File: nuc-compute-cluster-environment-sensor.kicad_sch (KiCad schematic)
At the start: 104 parts

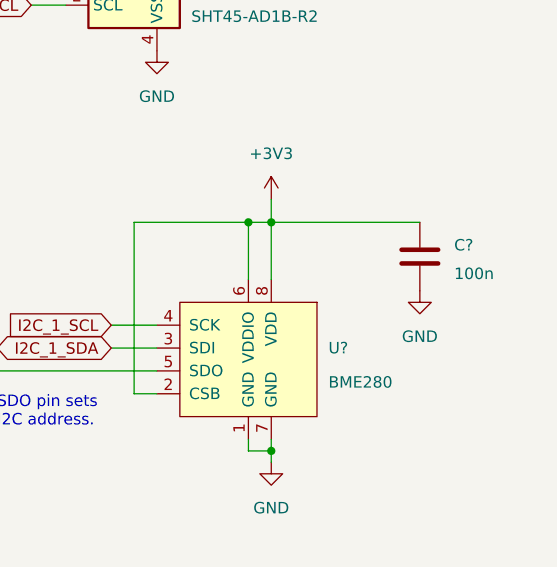
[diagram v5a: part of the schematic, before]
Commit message: [#39832] SCH: Add extra 100n cap to BME280 supply
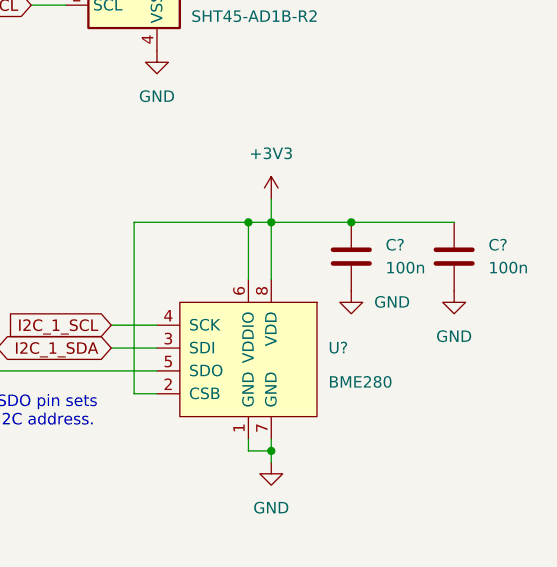
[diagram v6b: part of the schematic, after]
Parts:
- added C?: C_100n_0402, antmicro-footprints:0402-cap, symbol antmicroCapacitors0402:C_100n_0402
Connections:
- net +3V3: now also C?.2
- net GND: now also C?.1
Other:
- moved on the sheet: C?

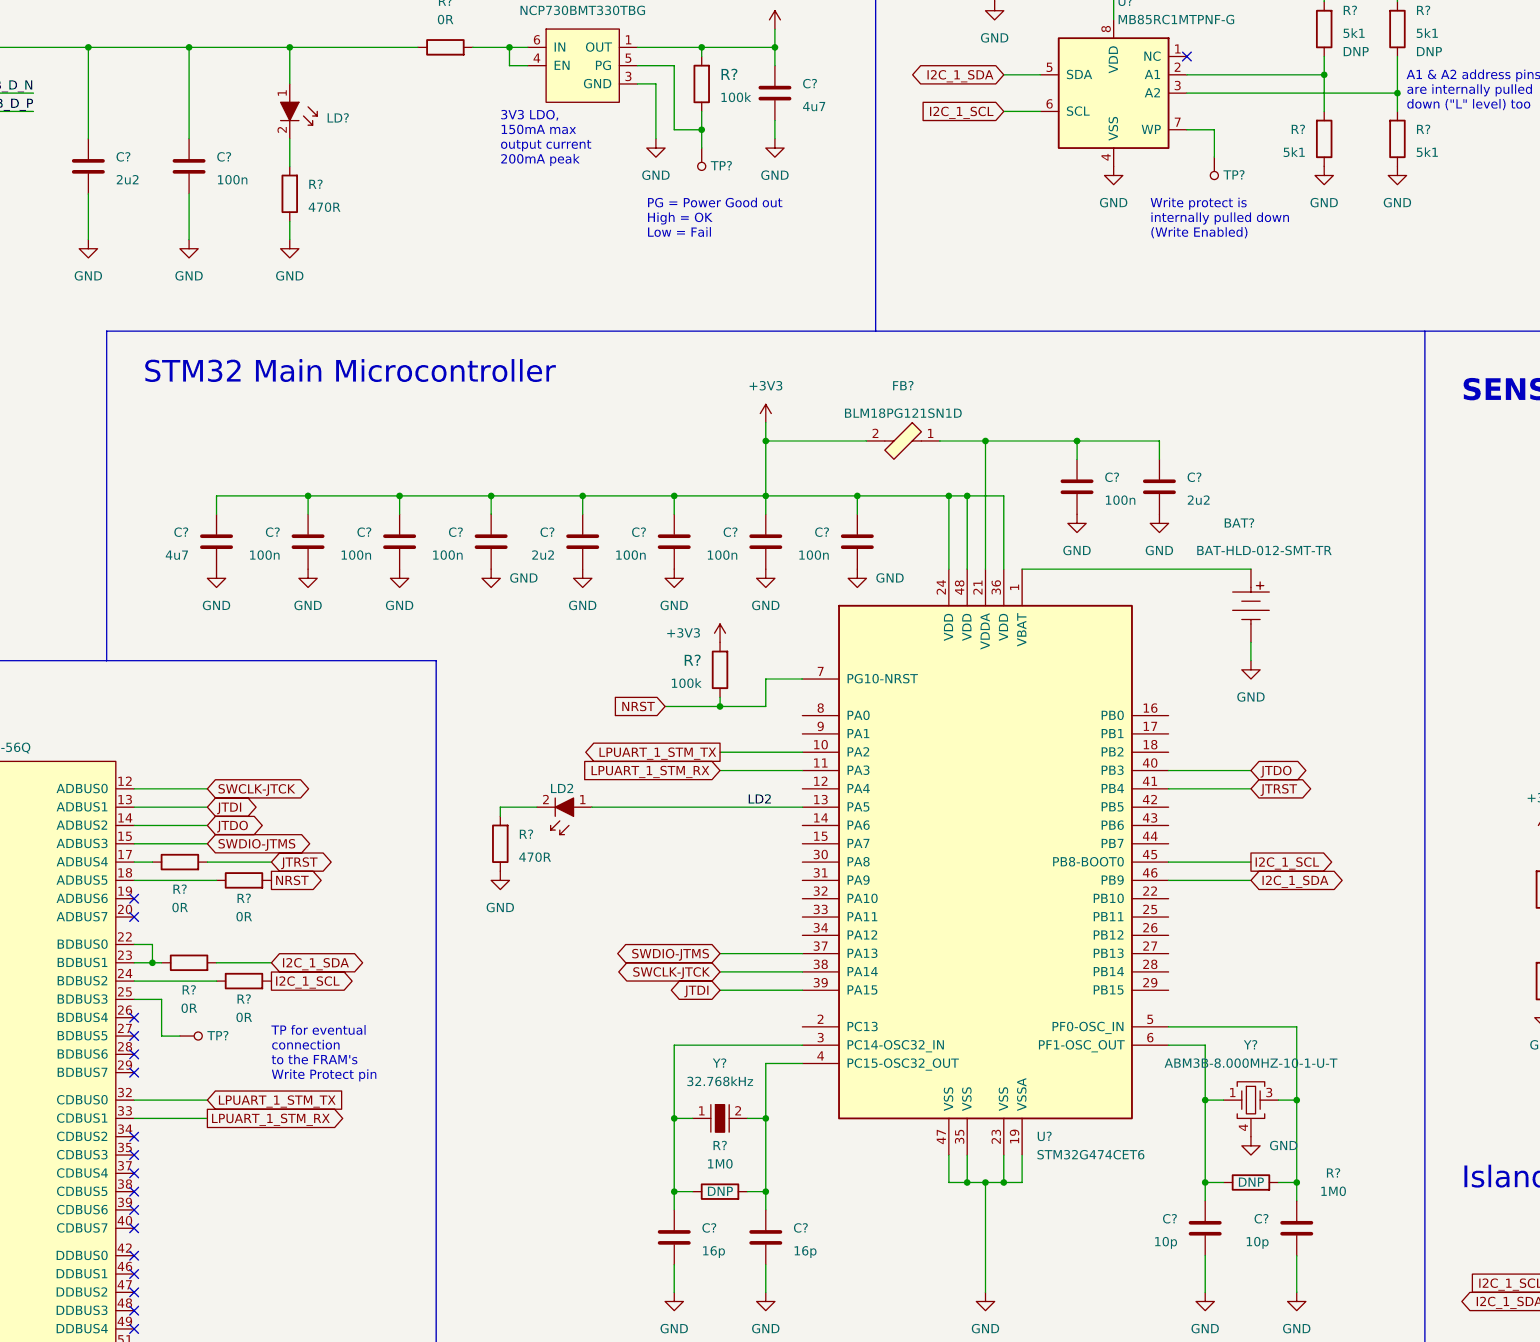
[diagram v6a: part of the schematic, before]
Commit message: [#39832] SCH: Fix FT4232H I2C connection, move FRAM Write Protect to BDBUS4
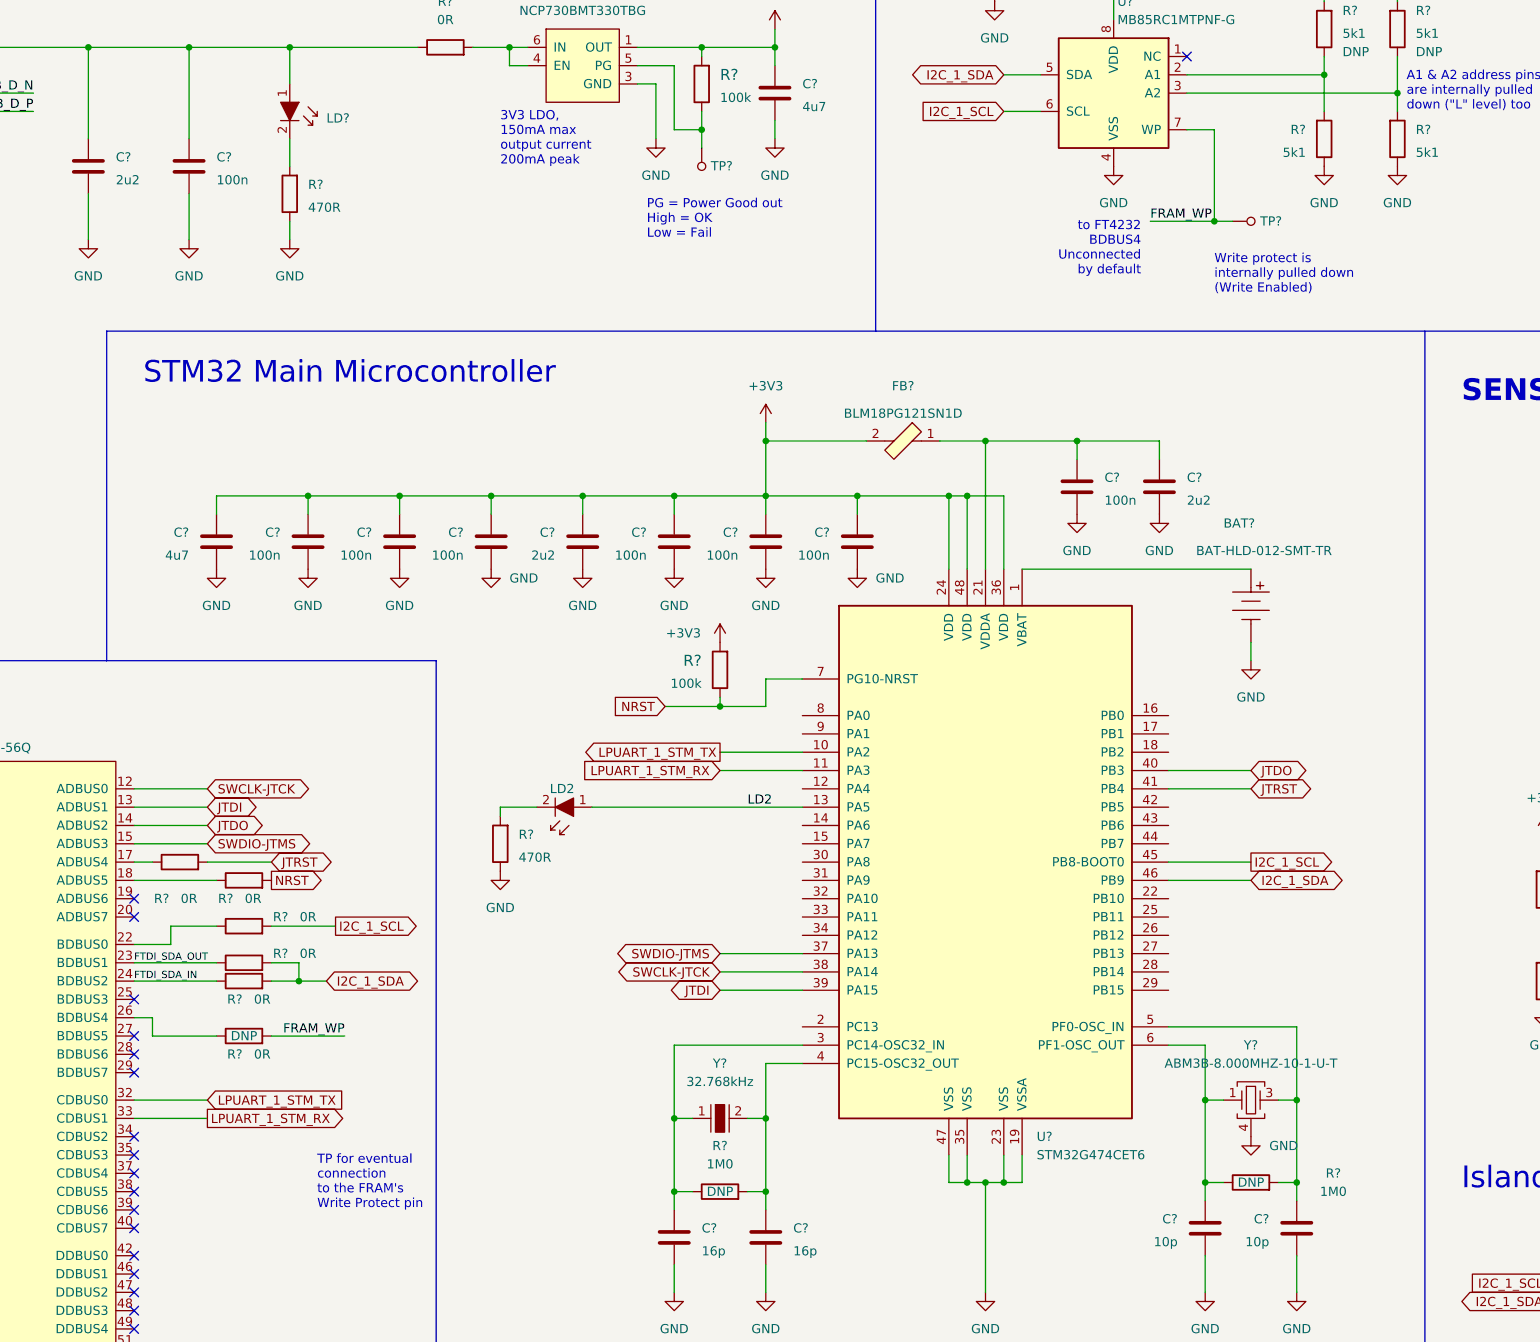
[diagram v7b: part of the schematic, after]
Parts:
- removed TP?: TP_SMD1MM, antmicro-footprints:Testpoint_smd_1mm, symbol antmicroTestPoints:TP_SMD1MM
- added R? (x2): R_0R_0402, antmicro-footprints:0402-res, symbol antmicroResistors0402:R_0R_0402
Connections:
- net I2C_1_SDA: now also R?.2
- net FRAM_WP: now reaches TP?.1, U?.7 (WP)
- net FRAM_WP: now also R?.2
- net FTDI_SDA_OUT: now reaches R?.1, U?.23 (BDBUS1)
- net FTDI_SDA_OUT: no longer U?.22 (BDBUS0)
- net at R?.1: now also U?.22 (BDBUS0); no longer U?.24 (BDBUS2)
- net at U?.26 (BDBUS4): now also R?.1
- new net FTDI_SDA_IN: R?.1, U?.24 (BDBUS2)
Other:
- note added: "to FT4232 BDBUS4 Unconnected by default"
- moved on the sheet: R?, TP?

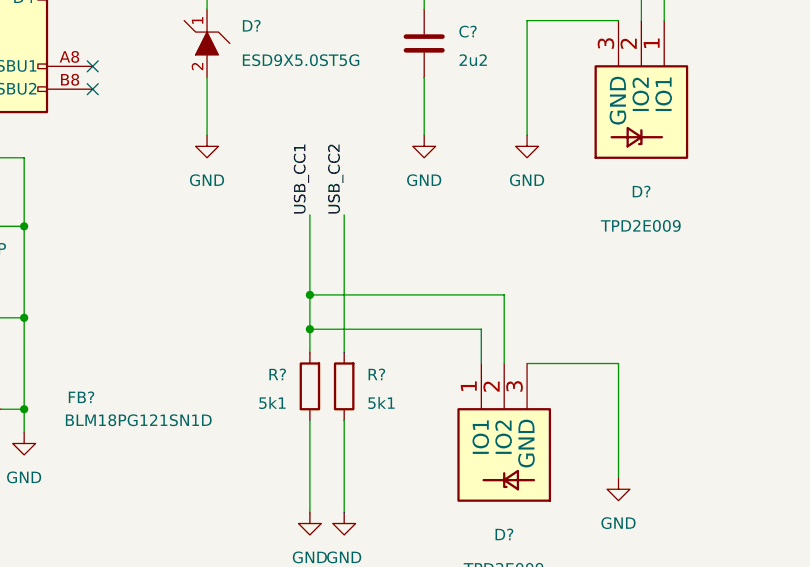
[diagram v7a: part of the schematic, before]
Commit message: [#39832] SCH: Fix USB_CC - ESD protetction TVSes miswiring
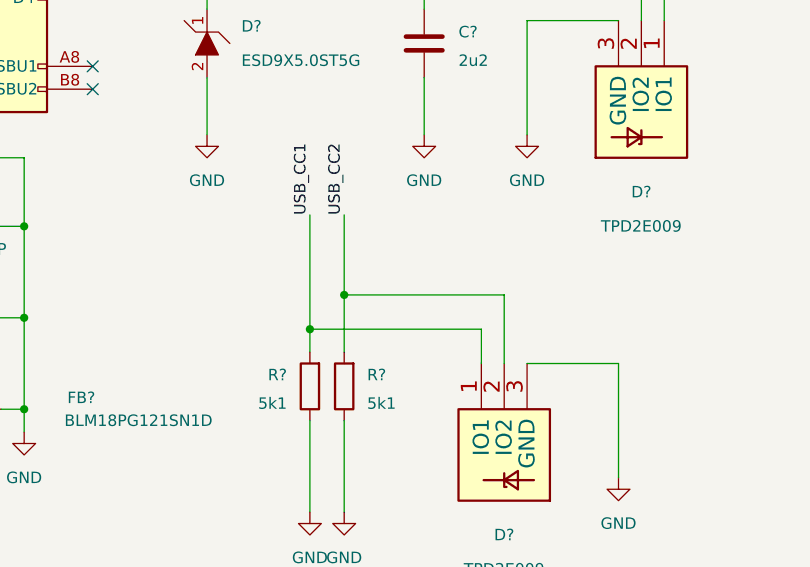
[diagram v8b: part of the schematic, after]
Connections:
- net USB_CC1: no longer D?.2 (IO2)
- net USB_CC2: now also D?.2 (IO2)
